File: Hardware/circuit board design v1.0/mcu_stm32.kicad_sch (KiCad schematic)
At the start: 31 parts, among them J1 Conn_01x02_Male, J4 DF13-10P-1.25DS_20_, J6 Conn_01x02_Male, Q1 2N7002-7-F, U1 STM32F446RETx, U2 W25Q64JVSS, U3 SDR08540M3-01, Y1 Crystal_GND24

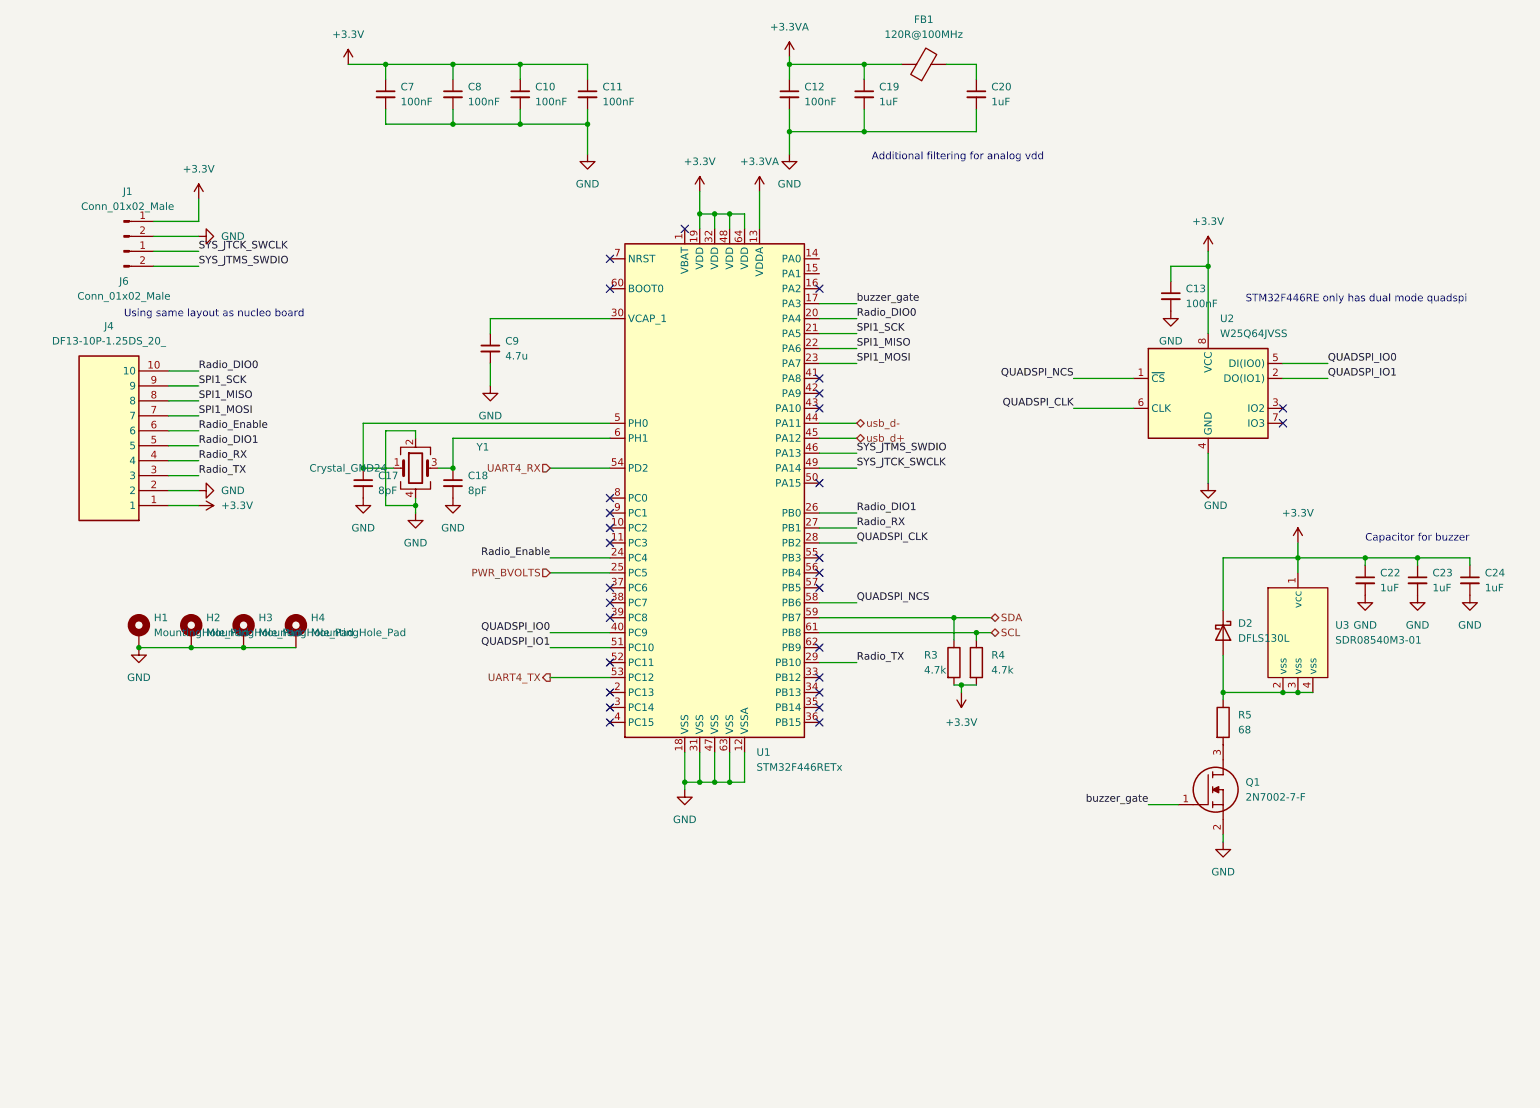
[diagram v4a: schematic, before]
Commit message: Added routing for radio module on back of pcb
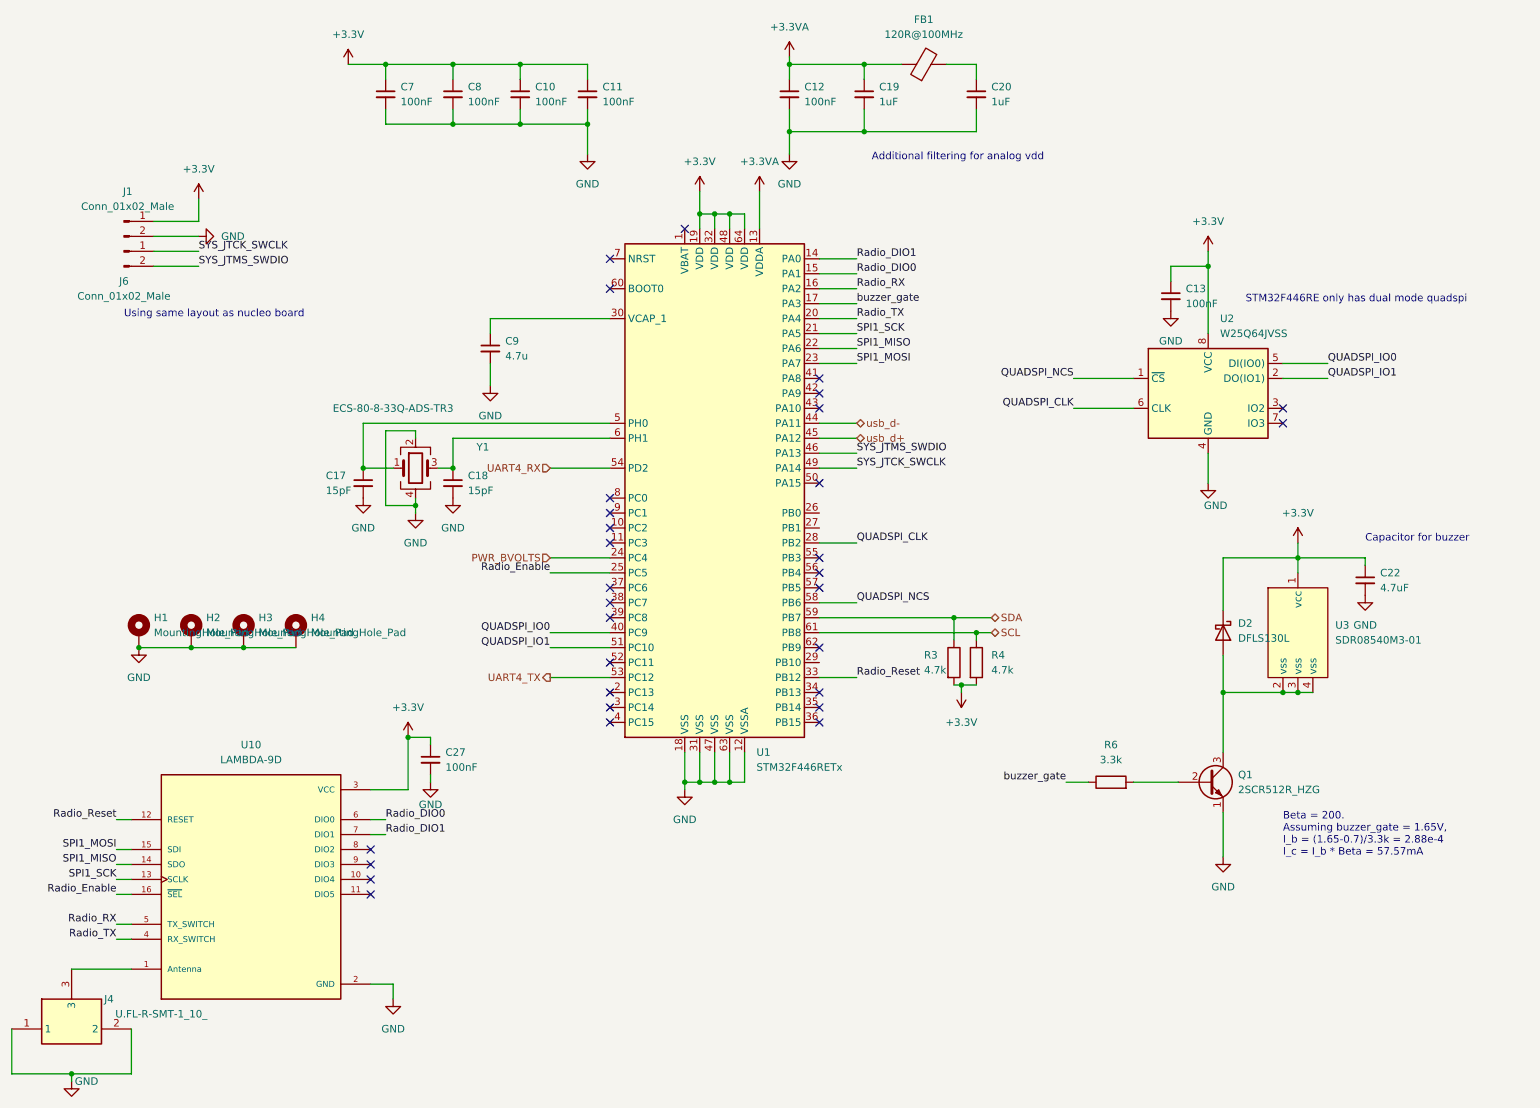
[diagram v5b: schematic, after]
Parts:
- removed C23, C24: 1uF, Capacitor_SMD:C_0603_1608Metric_Pad1.08x0.95mm_HandSolder, symbol Device:C_Small
- removed D2: DFLS130L, Components:PowerDI123, symbol Device:D_Schottky
- removed J4: DF13-10P-1.25DS_20_, Components:DF1310P125DS20, symbol Components:DF13-10P-1.25DS_20_
- removed Q1: 2N7002-7-F, Components:SOT96P240X120-3N, symbol Components:2N7002-7-F
- removed R5: 68, Resistor_SMD:R_0603_1608Metric, symbol Device:R
- added C27: 100nF, Capacitor_SMD:C_0603_1608Metric_Pad1.08x0.95mm_HandSolder, symbol Device:C_Small
- added D2: DFLS130L, Components:PowerDI123, symbol Components:DFLS130L
- added J4: U.FL-R-SMT-1_10_, Components:U.FL-R-SMT-1_10_, symbol Components:U.FL-R-SMT-1_10_
- added Q1: 2SCR512R_HZG, Components:2SCR512RHZG, symbol Components:2SCR512R_HZG
- added R6: 3.3k, Resistor_SMD:R_0603_1608Metric, symbol Device:R
- added U10: LAMBDA-9D, Components:XCVR_LAMBDA-9D, symbol Components:LAMBDA-9D
- C17, C18: value 8pF -> 15pF
- C19, C20: footprint Resistor_SMD:R_0603_1608Metric -> Capacitor_SMD:C_0603_1608Metric
- C22: value 1uF -> 4.7uF
- Y1: value Crystal_GND24 -> ECS-80-8-33Q-ADS-TR3
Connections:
- net +3.3V: now also C27.1, D2.1 (K), U10.3 (VCC)
- net GND: now also C27.2, J4.1, J4.2, Q1.1 (E), U10.2 (GND)
- net PWR_BVOLTS: now also U1.24 (PC4); no longer U1.25 (PC5)
- net Radio_DIO0: now also U1.15 (PA1), U10.6 (DIO0); no longer U1.20 (PA4)
- net Radio_DIO1: now also U1.14 (PA0), U10.7 (DIO1); no longer U1.26 (PB0)
- net Radio_Enable: now also U1.25 (PC5), U10.16 (~{SEL}); no longer U1.24 (PC4)
- net Radio_RX: now also U1.16 (PA2), U10.5 (TX_SWITCH); no longer U1.27 (PB1)
- net Radio_TX: now also U1.20 (PA4), U10.4 (RX_SWITCH); no longer U1.29 (PB10)
- net SPI1_MISO: now also U10.14 (SDO)
- net SPI1_MOSI: now also U10.15 (SDI)
- net SPI1_SCK: now also U10.13 (SCLK)
- net buzzer_gate: now also R6.1
- net at U3.2 (vss), U3.3 (vss), U3.4 (vss): now also D2.2 (A), Q1.3 (C)
- net Radio_Reset: now reaches U1.33 (PB12)
- net Radio_Reset: now also U10.12 (RESET)
- new net: J4.3, U10.1 (Antenna)
- new net: Q1.2 (B), R6.2
- no-connect marks 29 -> 31
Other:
- note added: "Beta = 200. Assuming buzzer_gate = 1.65V, I_b = (1.65-0.7)/3.3k = 2.88e-4 I_c = I_b * Beta = 57.57mA"
